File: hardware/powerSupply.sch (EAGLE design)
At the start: 49 parts, among them IC1 MCP3008, IC2 LM334Z, IC4 MCP4821P, J1 1X2-3.5MM, J2 1X2-3.5MM, T1 2N3904, T2 2N3904, U1 LM358, U2 LM358

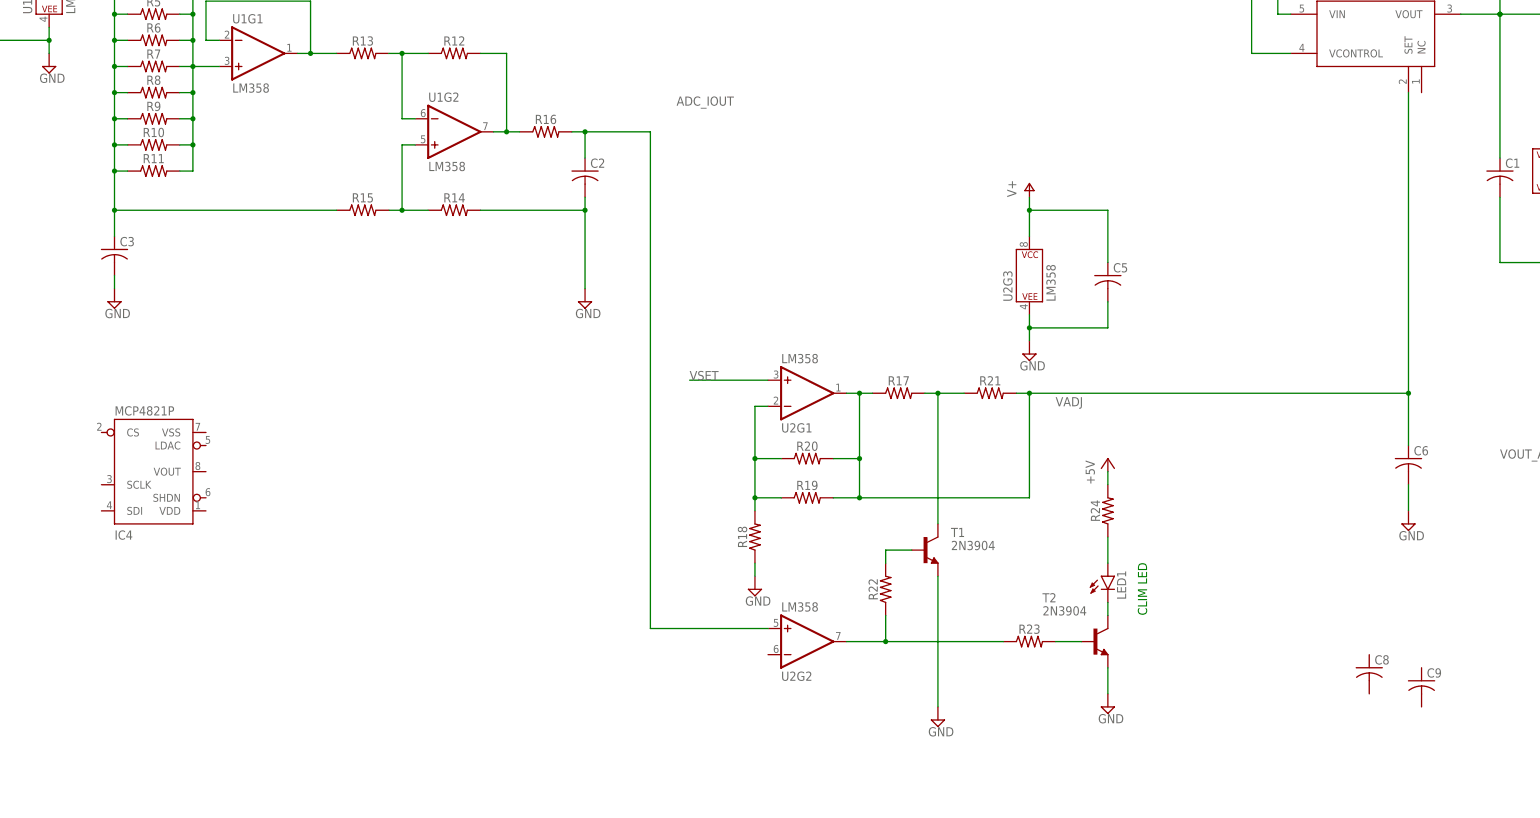
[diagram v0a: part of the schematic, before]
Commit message: 
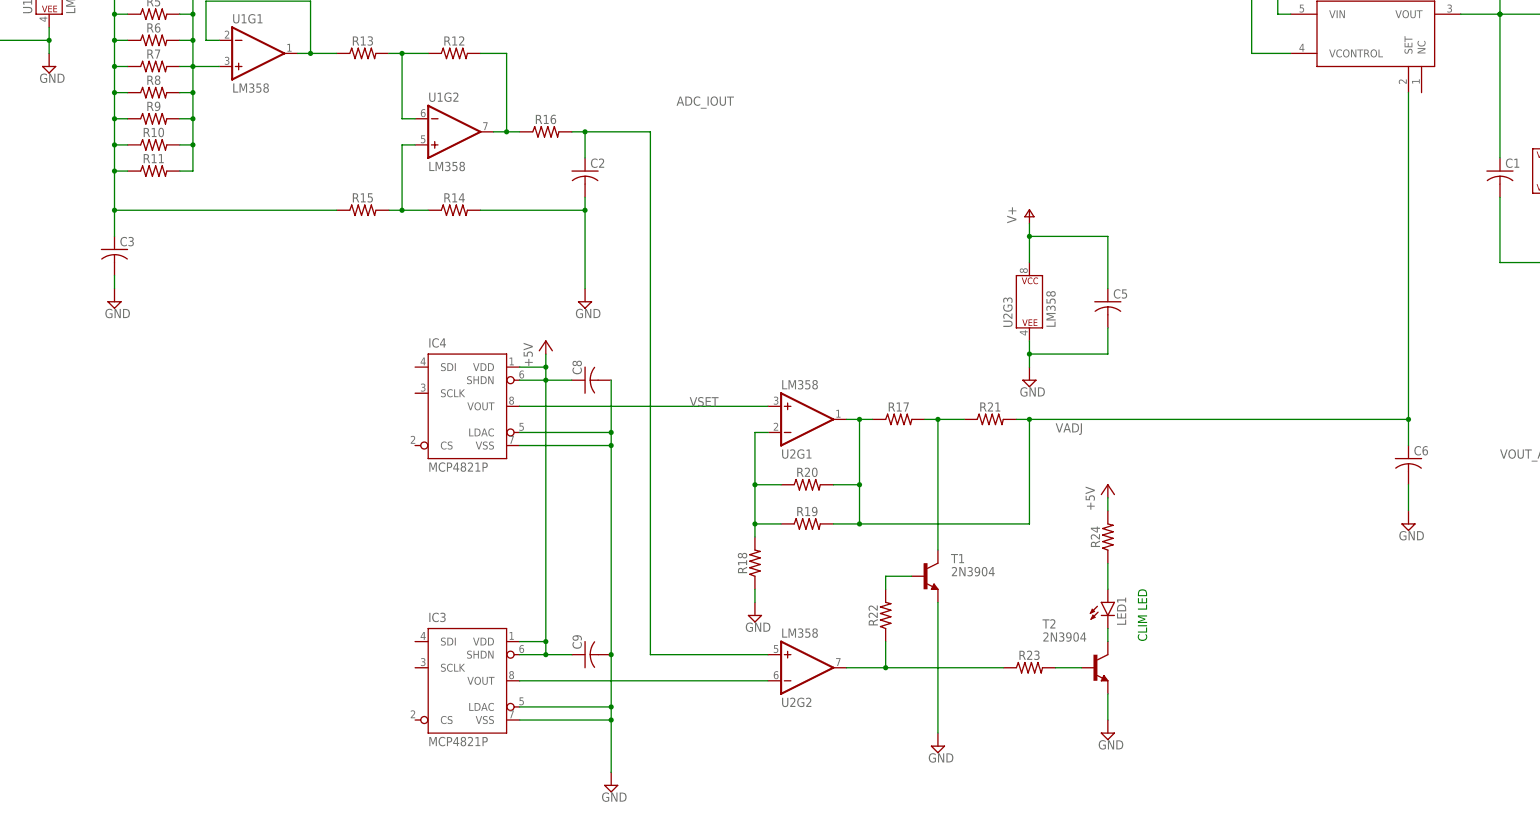
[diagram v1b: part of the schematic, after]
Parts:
- added IC3: MCP4821P, mixedSignal:MCP4821P
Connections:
- new net N$1: IC3.VOUT, U2G2.-IN
- net +5V: now also C8.1, C9.1, IC3.SHDN, IC3.VDD, IC4.SHDN, IC4.VDD
- net GND: now also C8.2, C9.2, IC3.LDAC, IC3.VSS, IC4.LDAC, IC4.VSS
- net VSET: now also IC4.VOUT
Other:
- moved on the sheet: C5, C8, C9, IC4, LED1, R17, R18, R19, R20, R21, R22, R23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

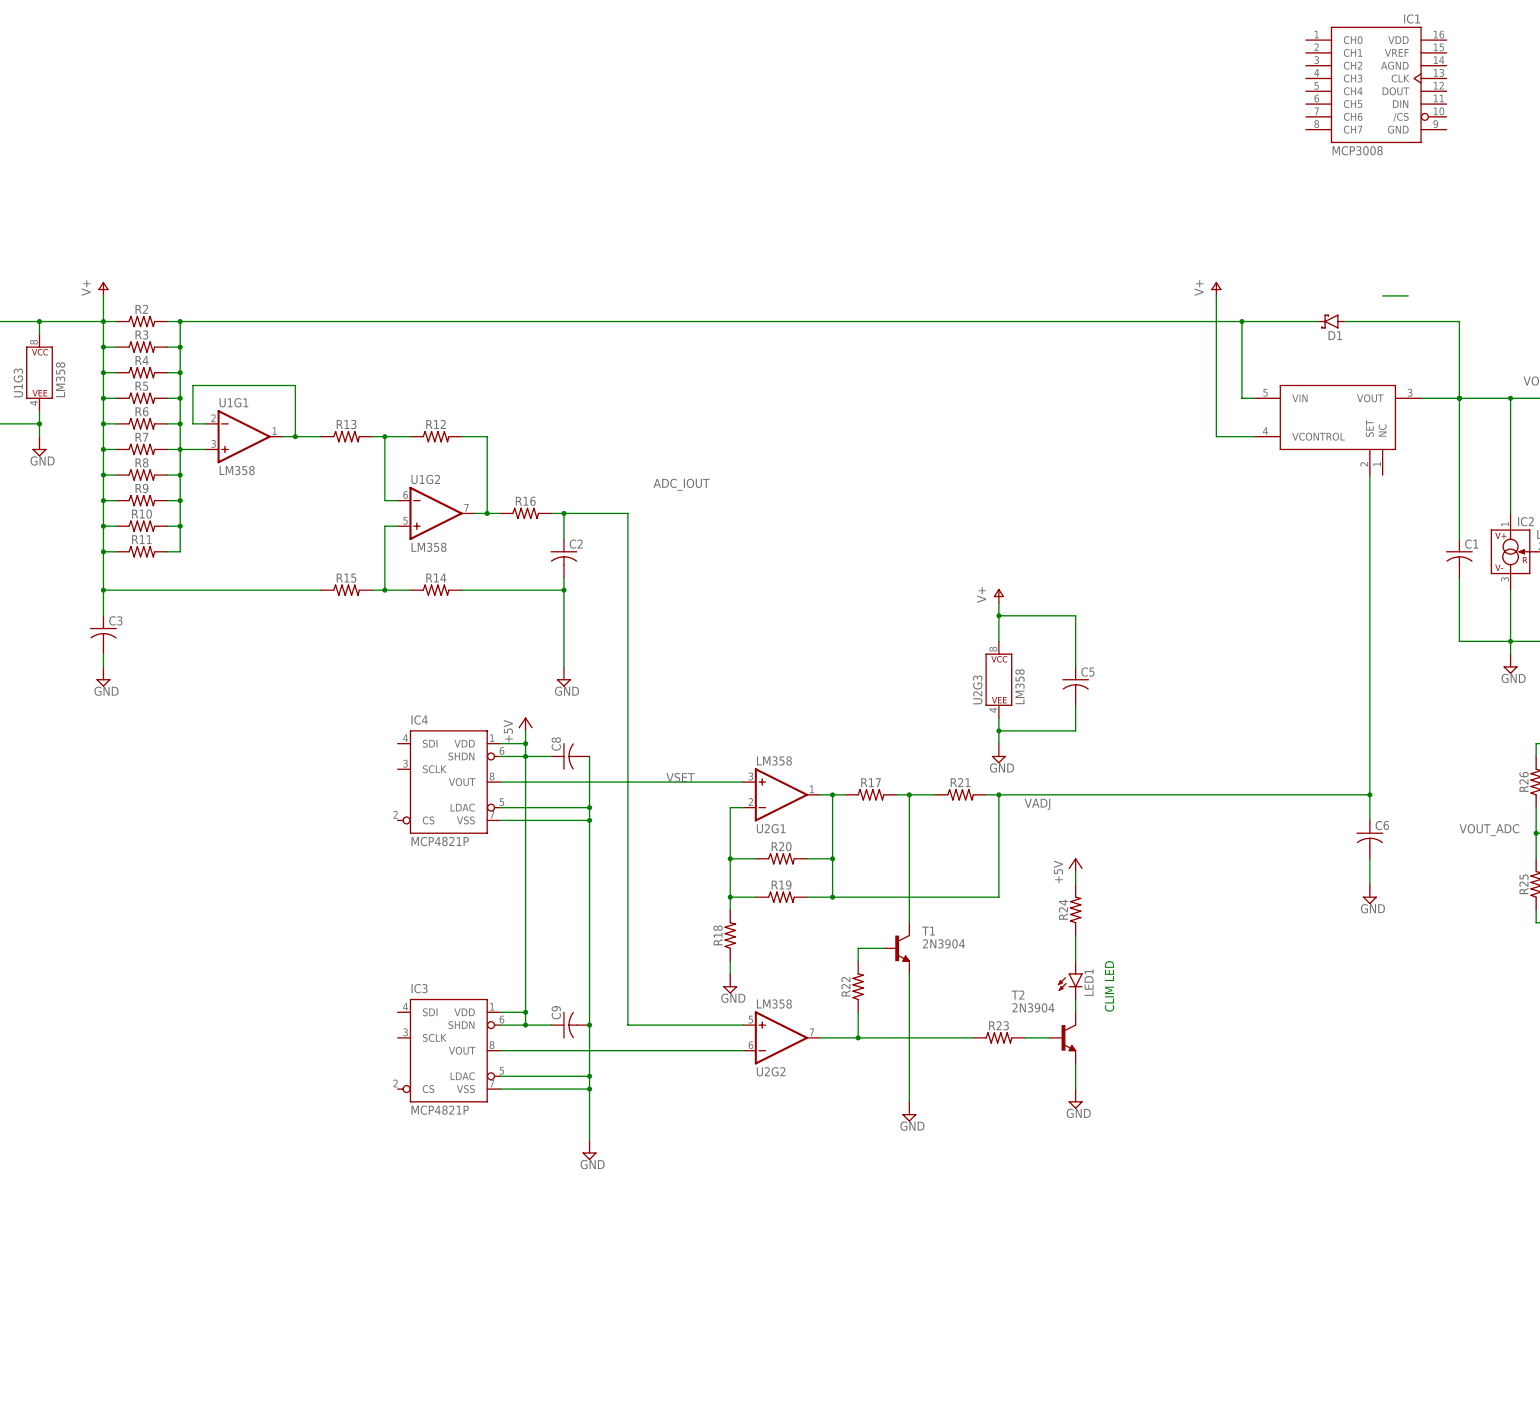
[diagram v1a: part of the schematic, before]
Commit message: 
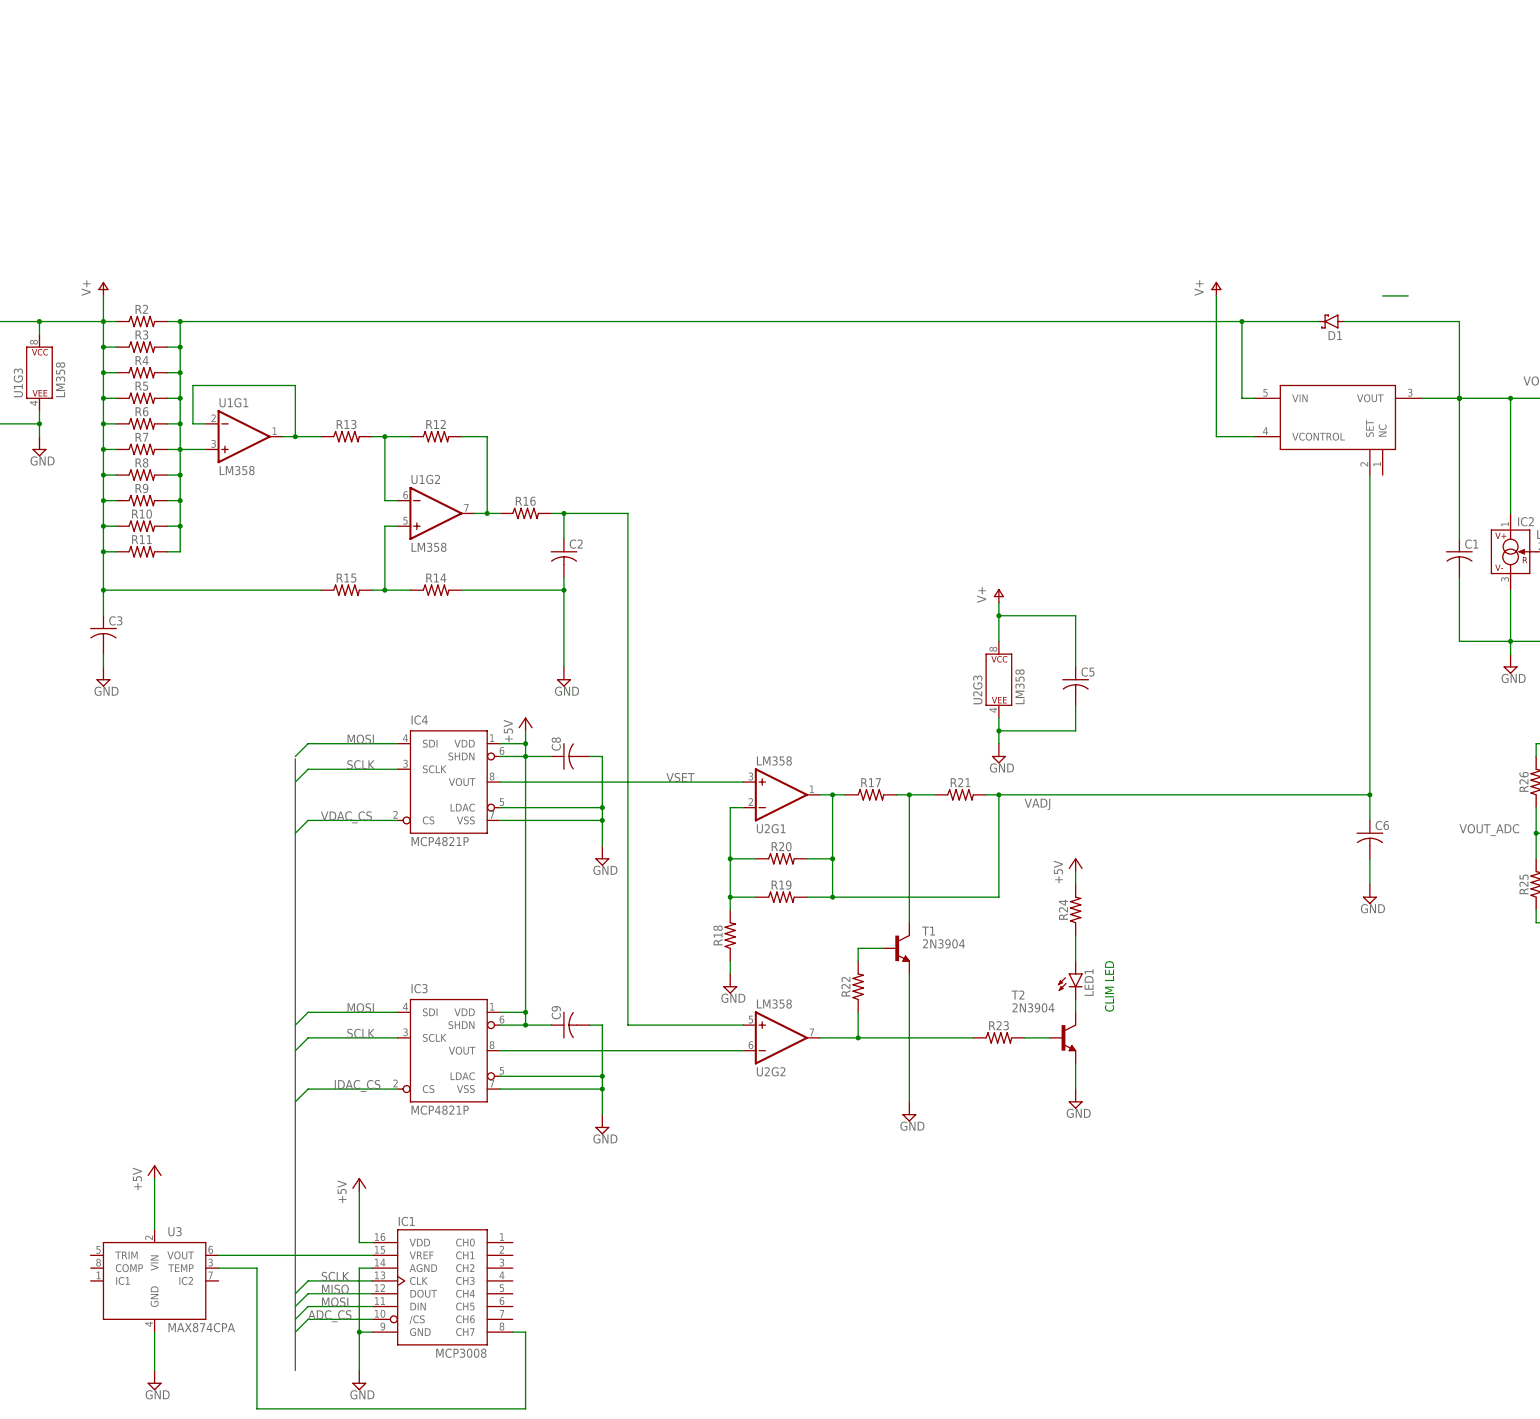
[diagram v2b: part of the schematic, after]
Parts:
- added U3: MAX874CPA, mixedSignal:MAX874CPA
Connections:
- new net ADC_CS: IC1./CS
- new net IDAC_CS: IC3.CS
- new net MISO: IC1.DOUT
- new net MOSI: IC1.DIN, IC3.SDI, IC4.SDI
- new net N$3: IC1.VREF, U3.VOUT
- new net N$5: IC1.CH7, U3.TEMP
- new net SCLK: IC1.CLK, IC3.SCLK, IC4.SCLK
- new net VDAC_CS: IC4.CS
- net +5V: now also IC1.VDD, U3.VIN
- net GND: now also IC1.AGND, IC1.GND, U3.GND
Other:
- moved on the sheet: IC1

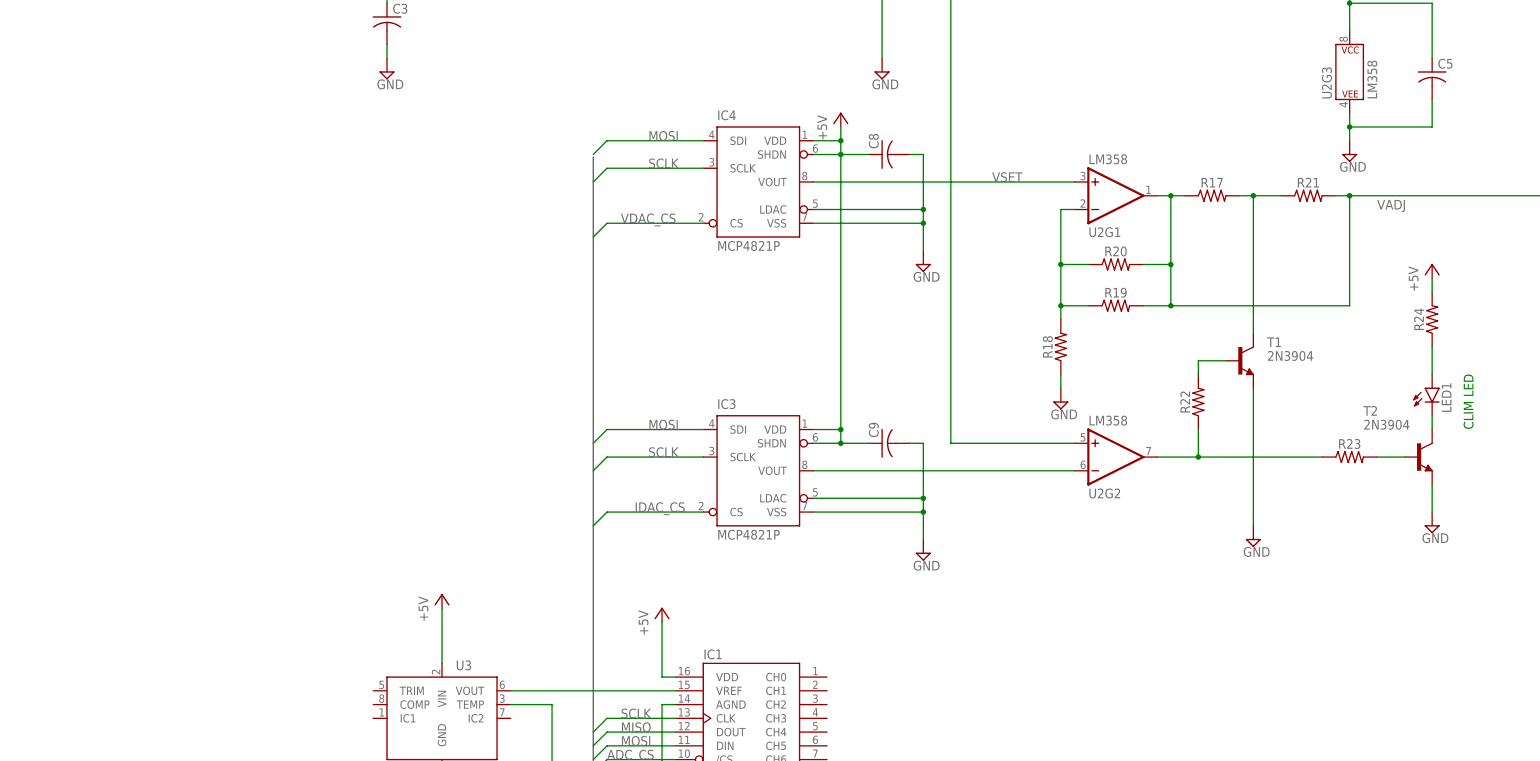
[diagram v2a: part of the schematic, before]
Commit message: 
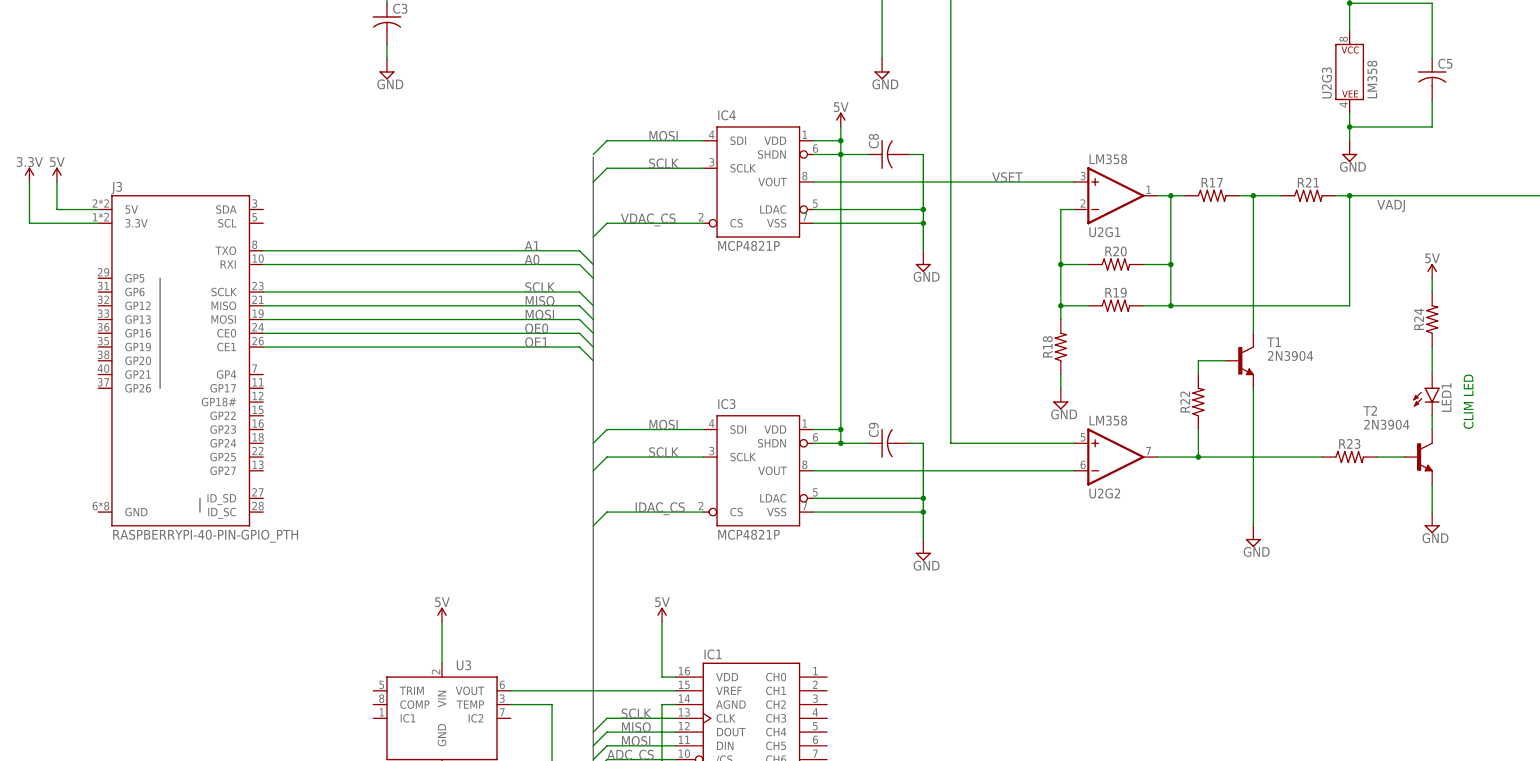
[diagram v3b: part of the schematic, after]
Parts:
- added J3: RASPBERRYPI-40-PIN-GPIO_PTH, SparkFun-Connectors:RASPBERRYPI-40-PIN-GPIO_PTH
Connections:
- removed net +5V: C8.1, C9.1, IC1.VDD, IC3.SHDN, IC3.VDD, IC4.SHDN, IC4.VDD, R24.2, U3.VIN
- new net 3.3V: J3.3.3V
- new net 5V: C8.1, C9.1, IC1.VDD, IC3.SHDN, IC3.VDD, IC4.SHDN, IC4.VDD, J3.5V, R24.2, U3.VIN
- new net A0: J3.RXI
- new net A1: J3.TXO
- new net OE0: J3.CE0
- new net OE1: J3.CE1
- net MISO: now also J3.MISO
- net MOSI: now also J3.MOSI
- net SCLK: now also J3.SCLK
